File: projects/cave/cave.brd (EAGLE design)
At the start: 100 x 72 mm, 113 parts, among them U1 IRLML6344TRPBF, U10 IRLML6344TRPBF, U11 IRLML6344TRPBF, U12 IRLML6344TRPBF, U2 TLC555CDR, U3 IRLML6344TRPBF, U4 IRLML6344TRPBF, U5 IRLML6344TRPBF, U6 IRLML6344TRPBF, U7 TPS54625, U9 IRLML6344TRPBF

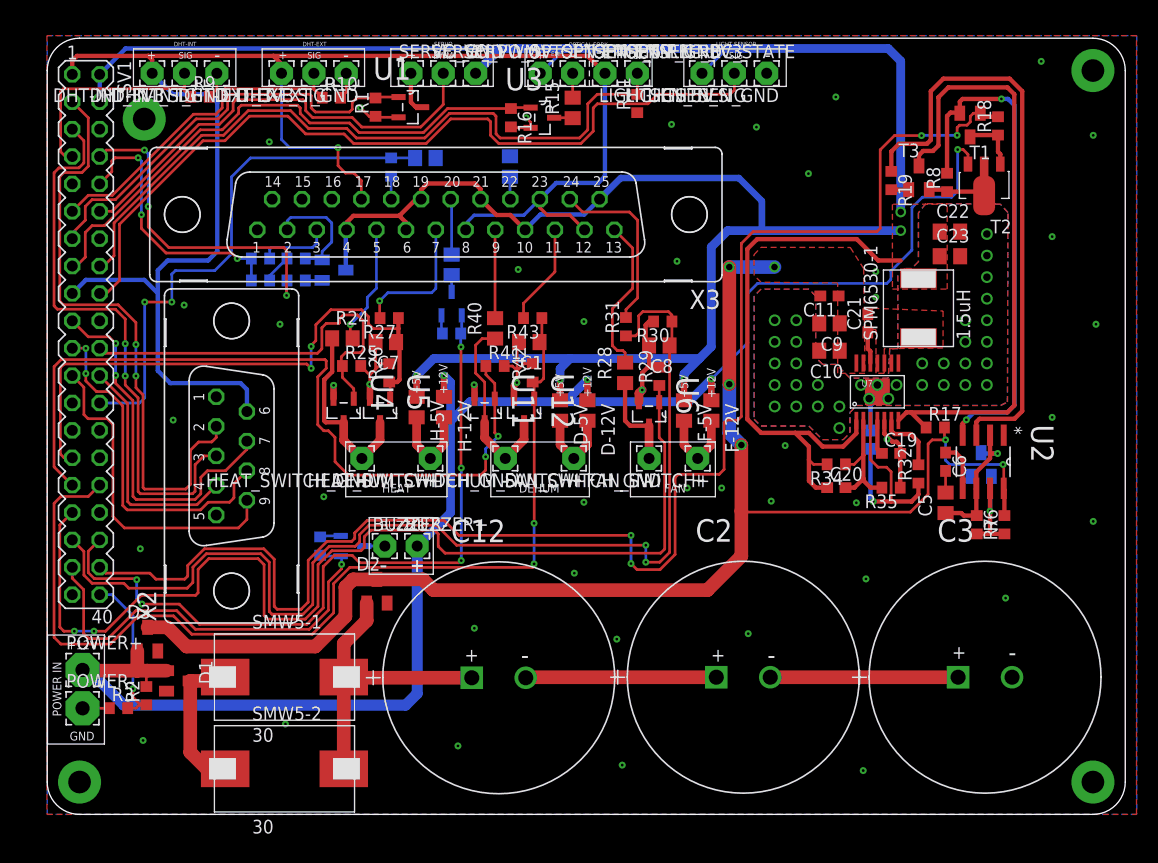
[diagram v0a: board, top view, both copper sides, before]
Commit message: Changed to Seeed's DRU -> min drill changed to 12mil (updated all vias)
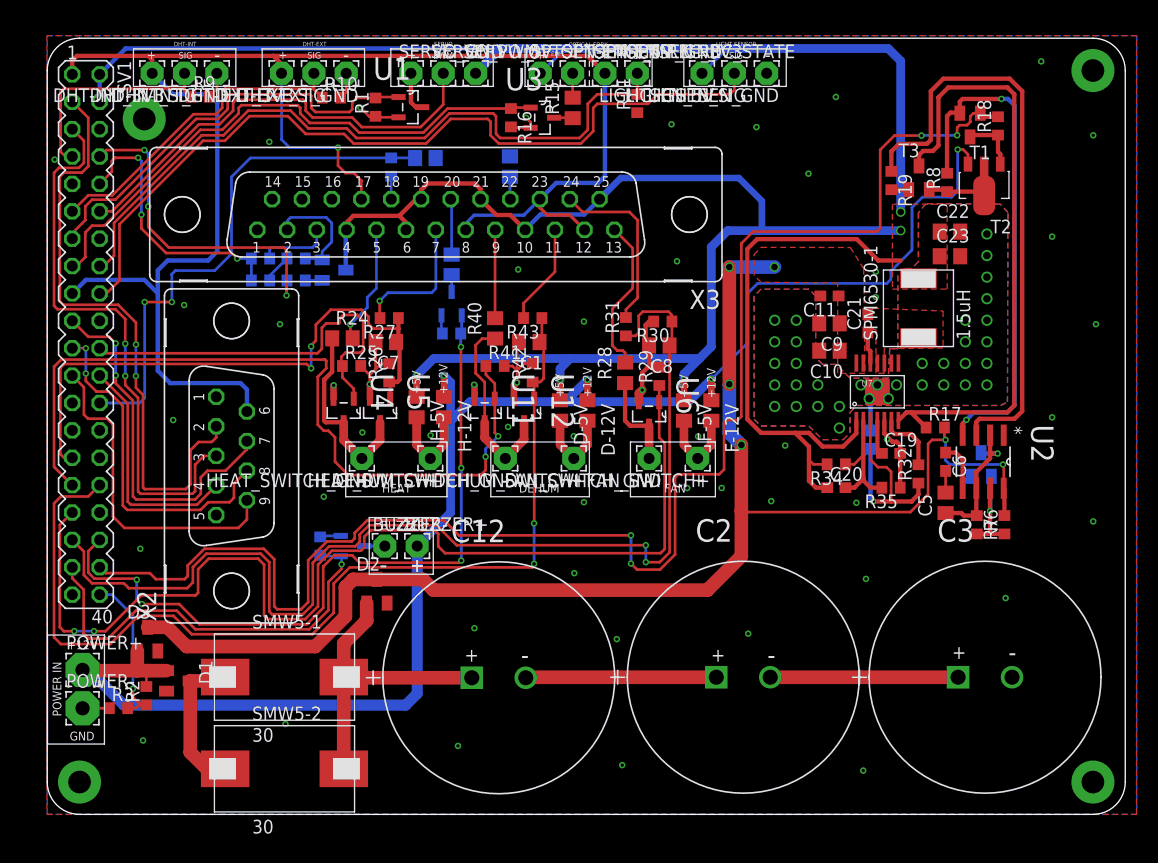
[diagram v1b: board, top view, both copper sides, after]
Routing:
- net GND: vias 85 -> 91

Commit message: Board dimension reduced to 99x70mm (Seeed's limitations). Gerber revA generated
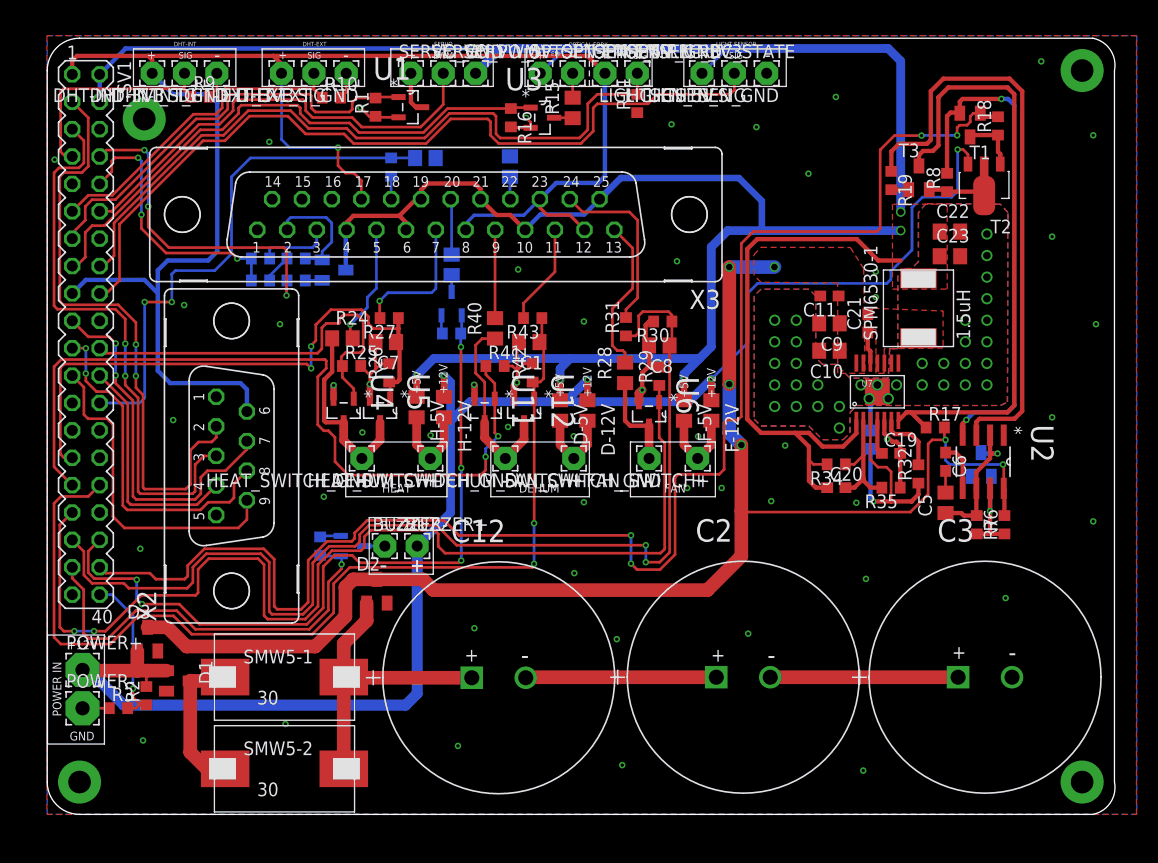
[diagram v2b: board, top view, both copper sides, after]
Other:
- board size 100 x 72 mm -> 99 x 72 mm
- board text added: "RevA"
- board text added: "T.MARION 11-2016"

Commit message: Changed wirepads positioning to keep the "GND-POW-SIG" pattern. Done some rerouting. tnames layer has to be clarified to be printed in the silkscreen.
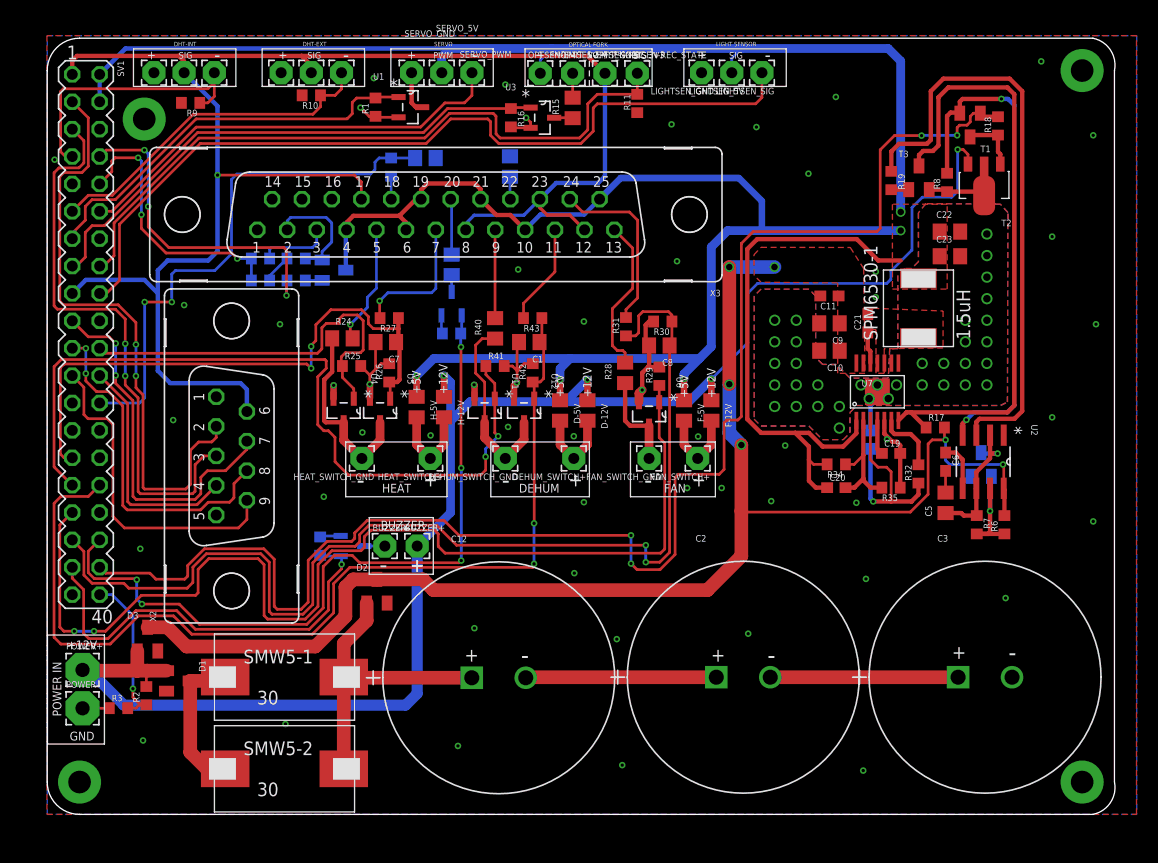
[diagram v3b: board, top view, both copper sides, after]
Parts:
- moved DHT-EXT_GND 6.04 mm to (21.7, 68.8)
- moved LIGHTSEN_GND 6.04 mm to (60.7, 68.8)
- moved DHT-INT_GND 5.84 mm to (9.90, 68.8)
- moved SERVO_5V 3.14 mm to (36.6, 68.8)
- moved DHT-INT_3V3 2.96 mm to (12.7, 68.8)
- moved DHT-EXT_3V3 2.76 mm to (24.5, 68.8)
- moved DHT-INT_SIG 2.76 mm to (15.5, 68.8)
- moved LIGHTSEN_5V 2.76 mm to (63.5, 68.8)
- moved SERVO_PWM 2.66 mm to (39.4, 68.8)
- moved DHT-EXT_SIG 2.56 mm to (27.3, 68.8)
- moved LIGHTSEN_SIG 2.56 mm to (66.3, 68.8)
- moved R10 1.88 mm to (24.5, 66.7), turned to 180 degrees
- moved R9 1.04 mm to (13.3, 66.0), turned to 180 degrees
- moved SERVO_GND 0.08 mm to (33.8, 68.8)
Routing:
- net +3V3: track 160.2 -> 154.5 mm
- net GND: track 67.2 -> 62.2 mm, vias 91 -> 92
- net DHT22_INT: track 21.8 -> 26.2 mm
- net +5V: track 278.3 -> 275.3 mm
- net OPTSEN_ON/OFF: track 52.6 -> 49.9 mm
- net SERVO_ON/OFF: track 39.9 -> 37.4 mm
- net OPTSEN_STATE: track 66.6 -> 64.5 mm
- net LIGHT_SENSOR: track 77.3 -> 78.2 mm
- net SERVO_PWM: track 41.9 -> 41.1 mm

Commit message: _tsilk moved to tDocu layer. tnames rearranged, silkscreen OK.
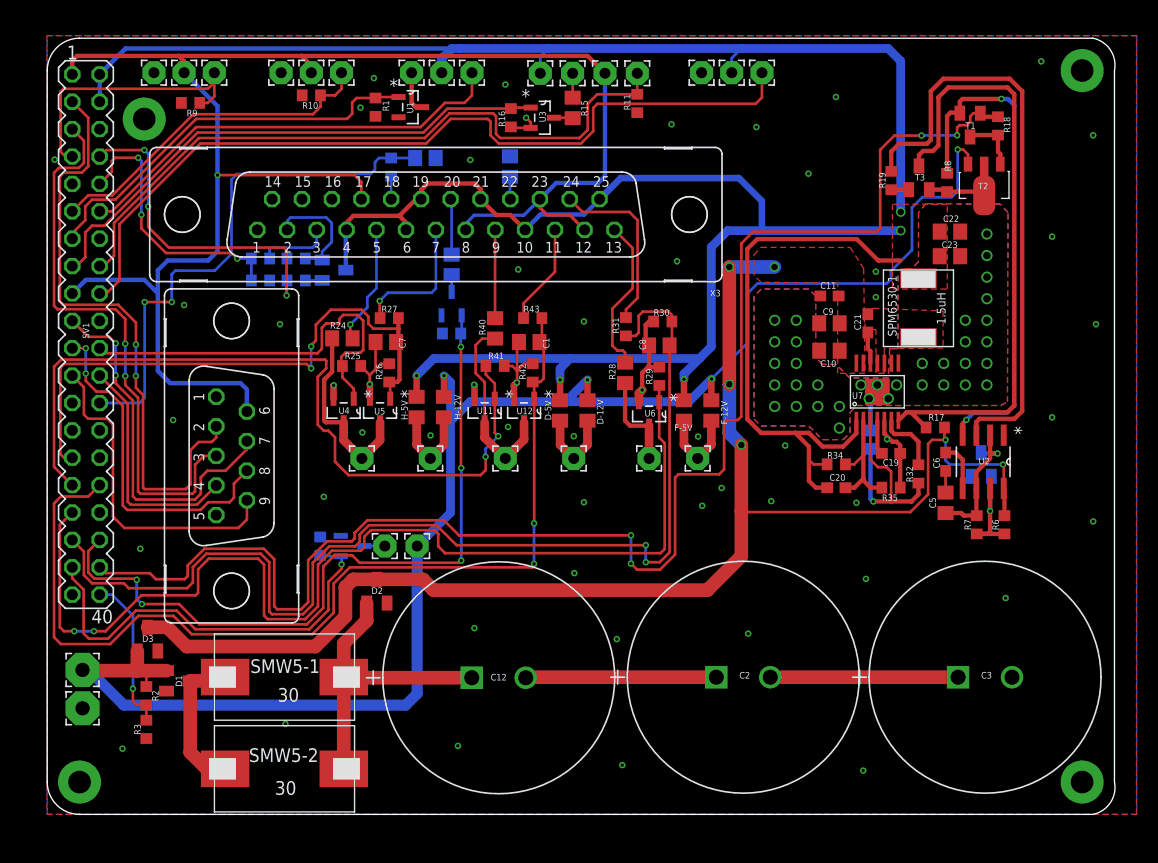
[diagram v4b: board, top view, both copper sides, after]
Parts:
- moved R3 3.24 mm to (9.19, 7.89), turned to 90 degrees
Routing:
- net GND: track 62.2 -> 49.5 mm, vias 92 -> 93

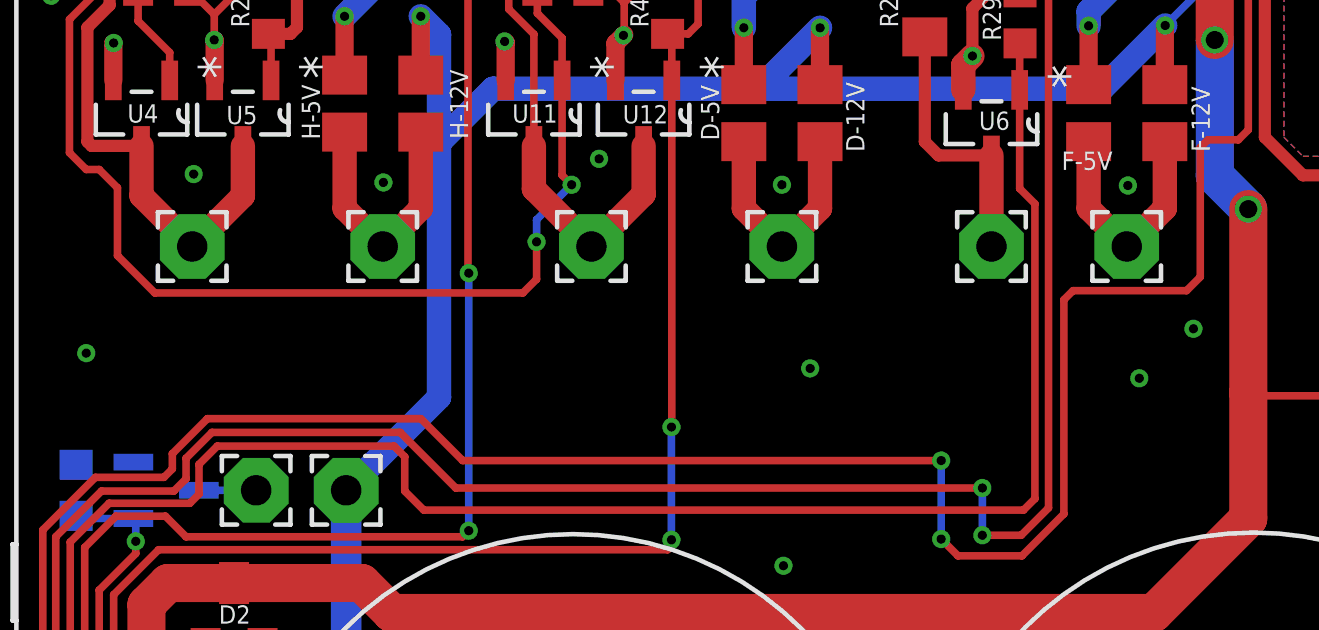
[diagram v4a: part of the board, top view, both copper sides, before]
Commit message: Added free wheel diode between the relays' terminal.
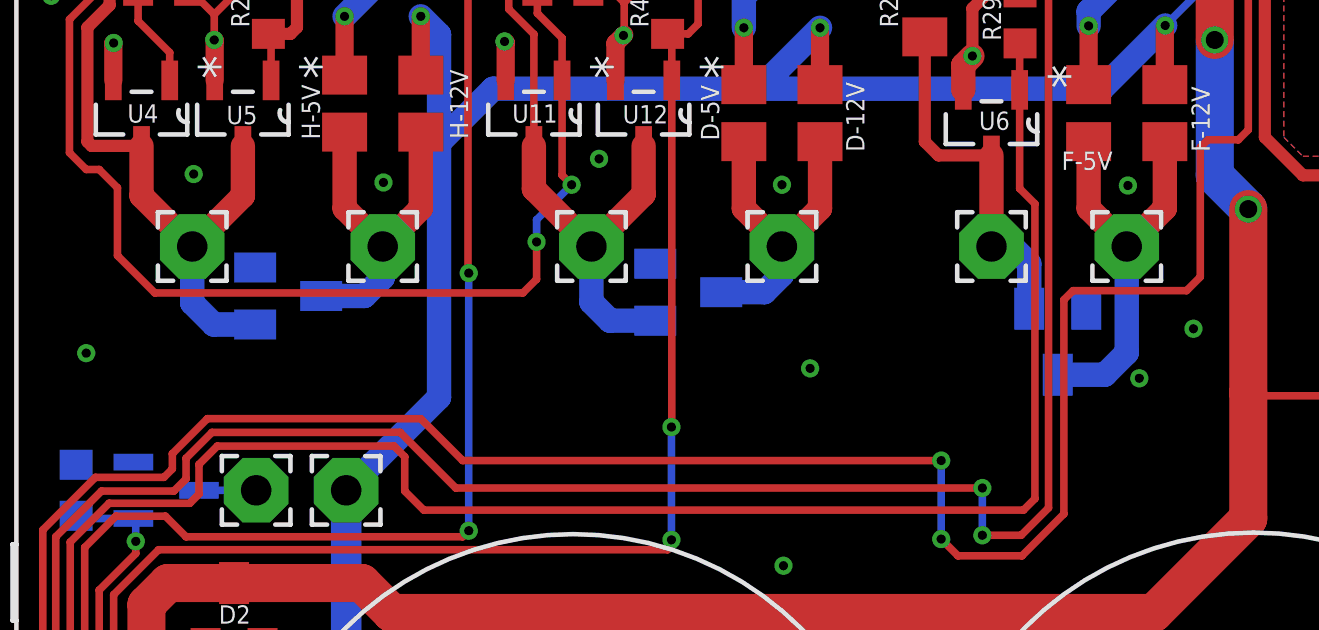
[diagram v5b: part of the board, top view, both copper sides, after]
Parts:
- added D5, D6, D7: SBR160S23-7, semicon-smd-ipc:SOT23
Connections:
- removed net N$21: HEAT_SWITCH_GND.1, R24.1, U4.3, U5.3
- removed net N$23: FAN_SWITCH_GND.1, R28.1, U6.3
- removed net N$24: DEHUM_SWITCH_GND.1, R40.1, U11.3, U12.3
- new net +12V1: D5.1, HEAT_SWITCH_GND.1, R24.1, U4.3, U5.3
- new net +12V2: D6.1, DEHUM_SWITCH_GND.1, R40.1, U11.3, U12.3
- new net +12V3: D7.1, FAN_SWITCH_GND.1, R28.1, U6.3
- net N$22: now also D7.3
- net N$26: now also D5.3
- net N$27: now also D6.3
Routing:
- net +12V1: track 0.00 -> 22.2 mm
- net +12V2: track 0.00 -> 22.0 mm
- net N$21: track 17.9 -> 0.00 mm
- net N$24: track 17.8 -> 0.00 mm
- net +12V3: track 0.00 -> 11.9 mm
- net N$23: track 8.94 -> 0.00 mm
- net N$22: track 8.04 -> 14.2 mm
- net N$26: track 8.68 -> 12.0 mm
- net N$27: track 8.04 -> 11.2 mm

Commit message: Fixed silkscreen error on top-board wirepads (forgot to update it after a81e98b). Changed some ill-named-nets' names for relays' GND.
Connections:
- net +12V1 renamed HEAT_GND
- net +12V2 renamed DEHUM_GND
- net +12V3 renamed FAN_GND
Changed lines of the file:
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@@
 <layer number="14" name="Route14" color="1" fill="6" visible="no" active="no"/>
 <layer number="15" name="Route15" color="4" fill="6" visible="no" active="no"/>
-<layer number="16" name="Bottom" color="1" fill="1" visible="yes" active="yes"/>
+<layer number="16" name="Bottom" color="1" fill="1" visible="no" active="yes"/>
 <layer number="17" name="Pads" color="2" fill="1" visible="yes" active="yes"/>
 <layer number="18" name="Vias" color="2" fill="1" visible="yes" active="yes"/>
-<layer number="19" name="Unrouted" color="6" fill="1" visible="yes" active="yes"/>
+<layer number="19" name="Unrouted" color="6" fill="1" visible="no" active="yes"/>
 <layer number="20" name="Dimension" color="15" fill="1" visible="yes" active="yes"/>
 <layer number="21" name="tPlace" color="7" fill="1" visible="yes" active="yes"/>
-<layer number="22" name="bPlace" color="7" fill="1" visible="yes" active="yes"/>
-<layer number="23" name="tOrigins" color="15" fill="1" visible="yes" active="yes"/>
-<layer number="24" name="bOrigins" color="15" fill="1" visible="yes" active="yes"/>
-<layer number="25" name="tNames" color="7" fill="1" visible="no" active="yes"/>
+<layer number="22" name="bPlace" color="7" fill="1" visible="no" active="yes"/>
+<layer number="23" name="tOrigins" color="15" fill="1" visible="no" active="yes"/>
+<layer number="24" name="bOrigins" color="15" fill="1" visible="no" active="yes"/>
+<layer number="25" name="tNames" color="7" fill="1" visible="yes" active="yes"/>
 <layer number="26" name="bNames" color="7" fill="1" visible="no" active="yes"/>
 <layer number="27" name="tValues" color="7" fill="1" visible="no" active="yes"/>
@@
 <layer number="45" name="Holes" color="7" fill="1" visible="no" active="yes"/>
 <layer number="46" name="Milling" color="3" fill="1" visible="no" active="yes"/>
-<layer number="47" name="Measures" color="7" fill="1" visible="yes" active="yes"/>
+<layer number="47" name="Measures" color="7" fill="1" visible="no" active="yes"/>
 <layer number="48" name="Document" color="7" fill="1" visible="no" active="yes"/>
 <layer number="49" name="Reference" color="7" fill="1" visible="no" active="yes"/>
 <layer number="50" name="dxf" color="7" fill="1" visible="no" active="no"/>
 <layer number="51" name="tDocu" color="7" fill="1" visible="yes" active="yes"/>
-<layer number="52" name="bDocu" color="7" fill="1" visible="yes" active="yes"/>
+<layer number="52" name="bDocu" color="7" fill="1" visible="no" active="yes"/>
 <layer number="53" name="tGND_GNDA" color="7" fill="9" visible="no" active="no"/>
 <layer number="54" name="bGND_GNDA" color="1" fill="9" visible="no" active="no"/>
@@
 <wire x1="17.5" y1="67.524" x2="8" y2="67.524" width="0.1" layer="51"/>
 <wire x1="8" y1="67.524" x2="8" y2="71.008" width="0.1" layer="51"/>
-<text x="9.246" y="70.048" size="0.8128" layer="51">+</text>
-<text x="12.192" y="70.104" size="0.6096" layer="51">SIG</text>
-<text x="15.494" y="69.85" size="1.27" layer="51">-</text>
+<text x="12.294" y="70.048" size="0.8128" layer="51">+</text>
+<text x="14.859" y="70.104" size="0.6096" layer="51">SIG</text>
+<text x="9.652" y="69.85" size="1.27" layer="51">-</text>
 <text x="23.692" y="71.254" size="0.4064" layer="51">DHT-EXT</text>
 <wire x1="19.938" y1="71.008" x2="29.438" y2="71.008" width="0.1" layer="51"/>
@@
 <wire x1="29.438" y1="67.524" x2="19.938" y2="67.524" width="0.1" layer="51"/>
 <wire x1="19.938" y1="67.524" x2="19.938" y2="71.008" width="0.1" layer="51"/>
-<text x="21.438" y="70.048" size="0.8128" layer="51">+</text>
-<text x="24.13" y="70.104" size="0.6096" layer="51">SIG</text>
-<text x="27.432" y="69.85" size="1.27" layer="51">-</text>
+<text x="24.105" y="70.048" size="0.8128" layer="51">+</text>
+<text x="26.67" y="70.104" size="0.6096" layer="51">SIG</text>
+<text x="21.463" y="69.85" size="1.27" layer="51">-</text>
 <text x="35.884" y="71.254" size="0.4064" layer="51">SERVO</text>
 <wire x1="31.876" y1="71.008" x2="41.376" y2="71.008" width="0.1" layer="51"/>
@@
 <wire x1="41.376" y1="67.524" x2="31.876" y2="67.524" width="0.1" layer="51"/>
 <wire x1="31.876" y1="67.524" x2="31.876" y2="71.008" width="0.1" layer="51"/>
-<text x="33.376" y="70.048" size="0.8128" layer="51">+</text>
-<text x="35.814" y="70.104" size="0.6096" layer="51">PWM</text>
-<text x="39.37" y="69.85" size="1.27" layer="51">-</text>
+<text x="36.17" y="70.048" size="0.8128" layer="51">+</text>
+<text x="38.481" y="70.104" size="0.6096" layer="51">PWM</text>
+<text x="33.401" y="69.85" size="1.27" layer="51">-</text>
 <text x="62.046" y="71.254" size="0.4064" layer="51">LIGHT SENSOR</text>
 <wire x1="59.054" y1="71.008" x2="68.554" y2="71.008" width="0.1" layer="51"/>
@@
 <wire x1="68.554" y1="67.524" x2="59.054" y2="67.524" width="0.1" layer="51"/>
 <wire x1="59.054" y1="67.524" x2="59.054" y2="71.008" width="0.1" layer="51"/>
-<text x="60.3" y="70.048" size="0.8128" layer="51">+</text>
-<text x="63.246" y="70.104" size="0.6096" layer="51">SIG</text>
-<text x="66.548" y="69.85" size="1.27" layer="51">-</text>
+<text x="63.094" y="70.048" size="0.8128" layer="51">+</text>
+<text x="65.659" y="70.104" size="0.6096" layer="51">SIG</text>
+<text x="60.325" y="69.85" size="1.27" layer="51">-</text>
 <text x="48.3554" y="71.2032" size="0.4064" layer="51">OPTICAL FORK</text>
 <wire x1="44.322" y1="71.008" x2="56.108" y2="71.008" width="0.1" layer="51"/>
@@
 <wire x1="31.9024" y1="57.0759" x2="31.9024" y2="59.1956" width="0.254" layer="16"/>
 </signal>
-<signal name="+12V1">
+<signal name="HEAT_GND">
 <contactref element="D5" pad="1"/>
 <contactref element="HEAT_SWITCH_GND" pad="1"/>
@@
 <wire x1="29.186" y1="31.139" x2="29.186" y2="33.0192" width="0.8128" layer="16"/>
 </signal>
-<signal name="+12V2">
+<signal name="DEHUM_GND">
 <contactref element="D6" pad="1"/>
 <contactref element="DEHUM_SWITCH_GND" pad="1"/>
@@
 <wire x1="42.4935" y1="31.1665" x2="42.4935" y2="33.0192" width="0.8128" layer="16"/>
 </signal>
-<signal name="+12V3">
+<signal name="FAN_GND">
 <contactref element="D7" pad="1"/>
 <contactref element="FAN_SWITCH_GND" pad="1"/>
